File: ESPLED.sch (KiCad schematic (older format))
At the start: 20 parts, among them CON1 BARREL_JACK, P1 PROG, P2 LED_CON, P3 LED_CON_SCREW, P4 LED_CON_SCREW, Q1 IRLZ34N, Q2 IRLZ34N, Q3 IRLZ34N, SW1 Reset, U1 LM1117-3.3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

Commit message: All coponents set
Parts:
- removed P1: PROG, Pin_Headers:Pin_Header_Straight_2x03_Pitch2.54mm, symbol CONN_02X03
- added D?: 1N5819, Diodes_THT:D_DO-41_SOD81_Horizontal_RM10, symbol 1N5819
- added J1: USB_B_Micro, symbol USB_B_Micro
- added R6, R7: R, symbol R
- added SW2: Program, symbol SW_Push
- added U3: INTERFACE-CH340T_SSOP20_, symbol INTERFACE-CH340T_SSOP20_
- added Y1: Crystal, symbol Crystal
- Q1, Q3: symbol Q_NMOS_DGS -> IRLZ34N
- R1, R2, R3: value 4.7k -> 100
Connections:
- net labels added: RXD, TXD, VUSB
- wire segments 60 -> 84
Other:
- moved on the sheet: C1, C2, C3, C4, CON1, P2, P3, P4, Q2, R1, R2, R3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

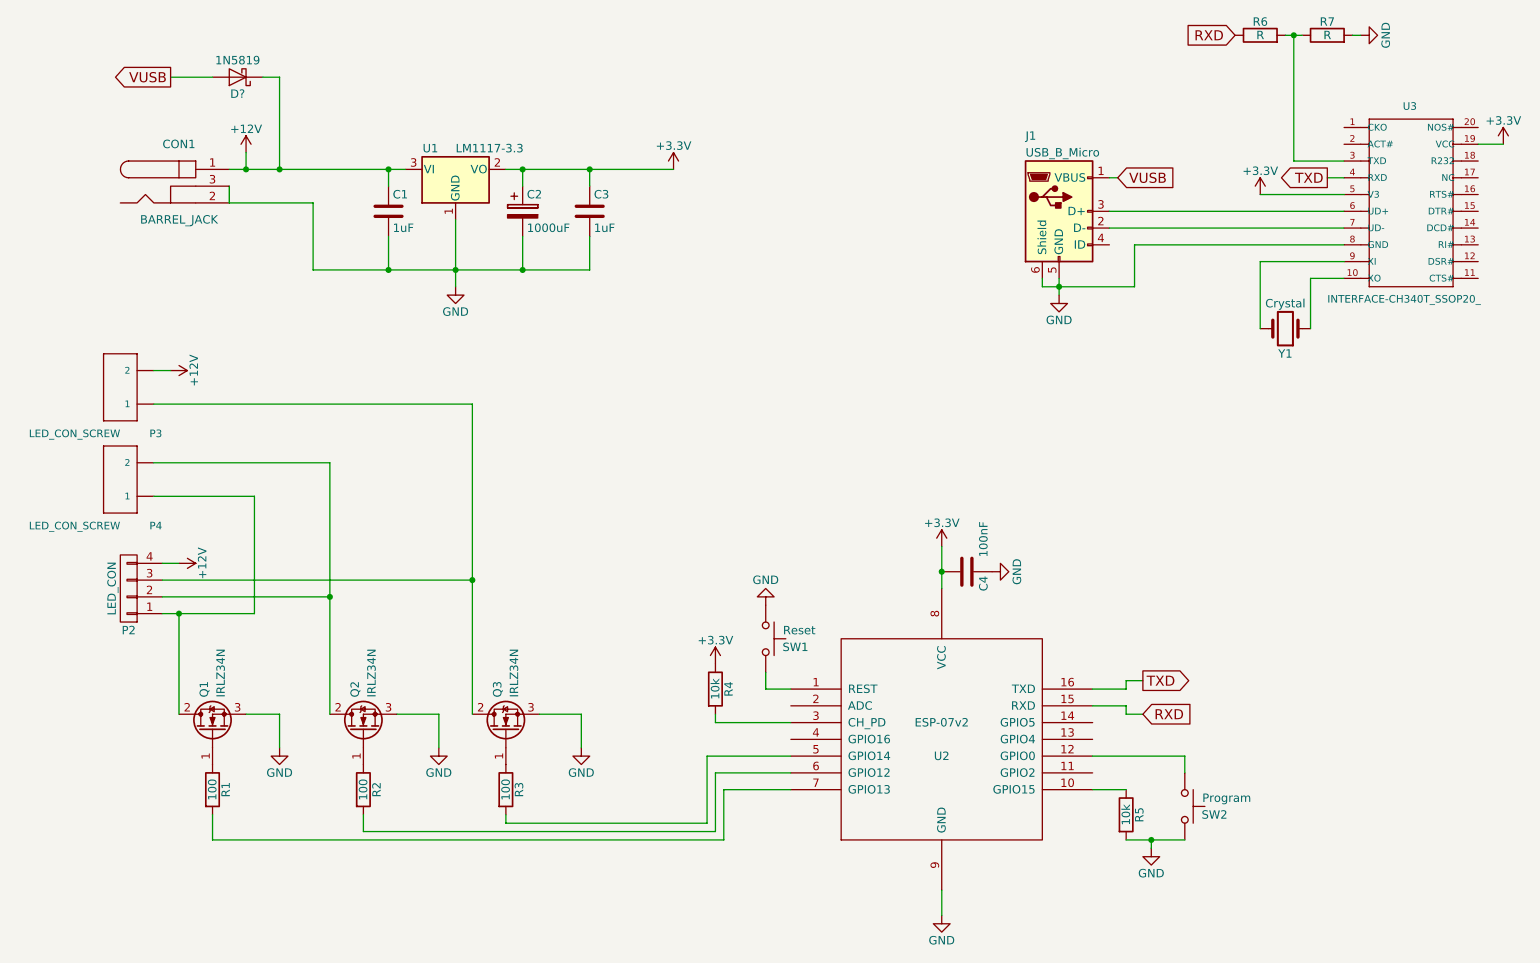
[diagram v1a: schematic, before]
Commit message: Added power suply switching circuit, cleaned up
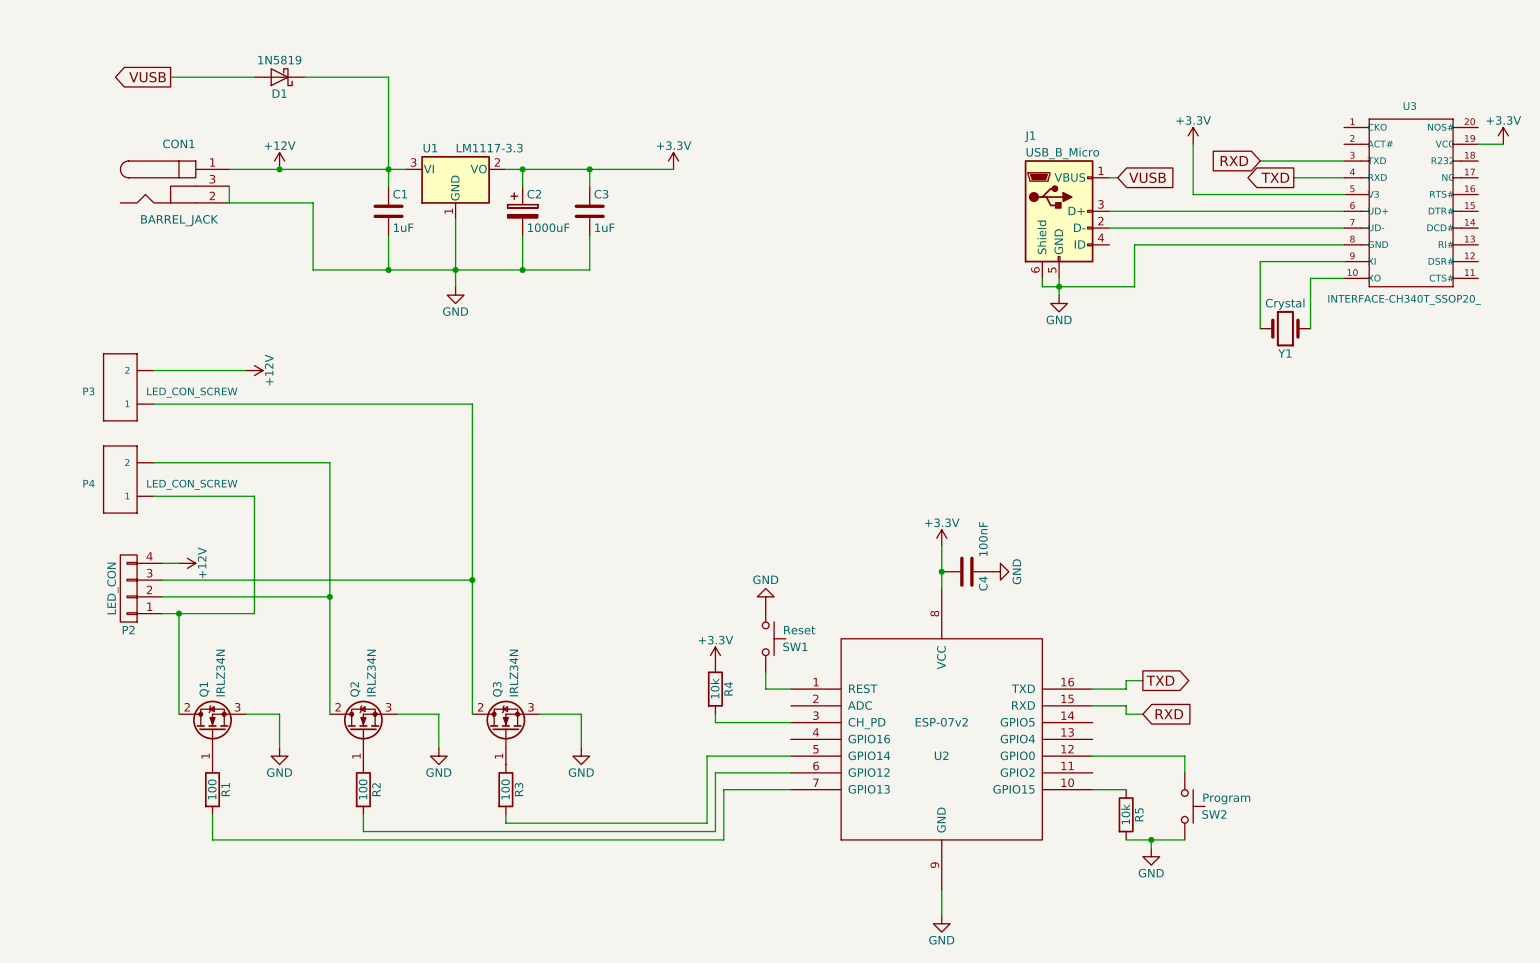
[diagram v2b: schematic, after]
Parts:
- removed R6, R7: R, symbol R
- gave numbers to parts that had none: 1
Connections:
- net RXD: now also U3.3 (TXD)
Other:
- moved on the sheet: D1
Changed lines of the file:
@@
 $EndComp
 Wire Wire Line
-	3050 1800 3050 1900
+	3050 1250 3050 1900
 Wire Wire Line
 	3050 2200 3050 2400
@@
 $EndComp
 Wire Wire Line
-	2100 1800 3150 1800
-Wire Wire Line
 	2100 2000 2600 2000
 Wire Wire Line
@@
 Wire Wire Line
 	6350 6100 6350 6250
-$Comp
-L +12V #PWR03
-U 1 1 5967C962
-P 2200 1700
-F 0 "#PWR03" H 2200 1550 50  0001 C CNN
-F 1 "+12V" H 2200 1840 50  0000 C CNN
-F 2 "" H 2200 1700 50  0000 C CNN
-F 3 "" H 2200 1700 50  0000 C CNN
-	1    2200 1700
-	1    0    0    -1
-$EndComp
 $Comp
 L +3.3V #PWR04
@@
 U 1 1 5A986FD8
 P 1450 3650
-F 0 "P4" H 1200 3900 45  0000 L BNN
-F 1 "LED_CON_SCREW" H 1450 3900 45  0000 L BNN
+F 0 "P4" H 1600 3650 45  0000 L BNN
+F 1 "LED_CON_SCREW" H 750 3650 45  0000 L BNN
 F 2 "SeeedOPL-Connector:H2-3.5-7.0X7.0MM" H 1450 3650 60  0001 C CNN
 F 3 "" H 1450 3650 60  0001 C CNN
@@
 U 1 1 5A987158
 P 1450 3100
-F 0 "P3" H 1200 3350 45  0000 L BNN
-F 1 "LED_CON_SCREW" H 1450 3350 45  0000 L BNN
+F 0 "P3" H 1600 3100 45  0000 L BNN
+F 1 "LED_CON_SCREW" H 750 3100 45  0000 L BNN
 F 2 "SeeedOPL-Connector:H2-3.5-7.0X7.0MM" H 1450 3100 60  0001 C CNN
 F 3 "" H 1450 3100 60  0001 C CNN
@@
 $EndComp
 Wire Wire Line
-	1650 3000 1750 3000
+	1650 3000 2200 3000
 Wire Wire Line
 	1650 3200 3550 3200
@@
 Wire Wire Line
 	7450 5000 7250 5000
-Text GLabel 8650 1850 0    60   Output ~ 0
+Text GLabel 8450 1850 0    60   Output ~ 0
 TXD
-Text GLabel 8100 1000 0    60   Input ~ 0
+Text GLabel 8250 1750 0    60   Input ~ 0
 RXD
-$Comp
-L R R6
-U 1 1 5BF92A24
-P 8250 1000
-F 0 "R6" V 8330 1000 50  0000 C CNN
-F 1 "R" V 8250 1000 50  0000 C CNN
-F 2 "" V 8180 1000 50  0001 C CNN
-F 3 "" H 8250 1000 50  0001 C CNN
-	1    8250 1000
-	0    -1   -1   0
-$EndComp
-$Comp
-L R R7
-U 1 1 5BF92B09
-P 8650 1000
-F 0 "R7" V 8730 1000 50  0000 C CNN
-F 1 "R" V 8650 1000 50  0000 C CNN
-F 2 "" V 8580 1000 50  0001 C CNN
-F 3 "" H 8650 1000 50  0001 C CNN
-	1    8650 1000
-	0    -1   -1   0
-$EndComp
-$Comp
-L GND #PWR015
-U 1 1 5BF92C41
-P 8850 1000
-F 0 "#PWR015" H 8850 750 50  0001 C CNN
-F 1 "GND" H 8850 850 50  0000 C CNN
-F 2 "" H 8850 1000 50  0001 C CNN
-F 3 "" H 8850 1000 50  0001 C CNN
-	1    8850 1000
-	0    -1   -1   0
-$EndComp
-Wire Wire Line
-	8800 1000 8850 1000
-Wire Wire Line
-	8400 1000 8500 1000
-Wire Wire Line
-	8450 1000 8450 1750
-Wire Wire Line
-	8450 1750 8750 1750
-Connection ~ 8450 1000
-Wire Wire Line
-	8650 1850 8750 1850
+Wire Wire Line
+	8450 1850 8750 1850
 Wire Wire Line
 	9700 1650 9550 1650
@@
 	8250 2350 8750 2350
 Wire Wire Line
-	8250 1950 8750 1950
+	7850 1950 8750 1950
 Text GLabel 7400 1850 2    60   Input ~ 0
 VUSB
@@
 L +3.3V #PWR?
 U 1 1 5BF96A99
-P 8250 1950
-F 0 "#PWR?" H 8250 1800 50  0001 C CNN
-F 1 "+3.3V" H 8250 2090 50  0000 C CNN
-F 2 "" H 8250 1950 50  0001 C CNN
-F 3 "" H 8250 1950 50  0001 C CNN
-	1    8250 1950
-	1    0    0    -1
-$EndComp
-$Comp
-L 1N5819 D?
+P 7850 1650
+F 0 "#PWR?" H 7850 1500 50  0001 C CNN
+F 1 "+3.3V" H 7850 1790 50  0000 C CNN
+F 2 "" H 7850 1650 50  0001 C CNN
+F 3 "" H 7850 1650 50  0001 C CNN
+	1    7850 1650
+	1    0    0    -1
+$EndComp
+$Comp
+L 1N5819 D1
 U 1 1 5BF96FE8
-P 2150 1250
-F 0 "D?" H 2150 1350 50  0000 C CNN
-F 1 "1N5819" H 2150 1150 50  0000 C CNN
-F 2 "Diodes_THT:D_DO-41_SOD81_Horizontal_RM10" H 2150 1075 50  0001 C CNN
-F 3 "" H 2150 1250 50  0001 C CNN
-	1    2150 1250
+P 2400 1250
+F 0 "D1" H 2400 1350 50  0000 C CNN
+F 1 "1N5819" H 2400 1150 50  0000 C CNN
+F 2 "Diodes_THT:D_DO-41_SOD81_Horizontal_RM10" H 2400 1075 50  0001 C CNN
+F 3 "" H 2400 1250 50  0001 C CNN
+	1    2400 1250
 	-1   0    0    1
 $EndComp
 Wire Wire Line
-	1750 1250 2000 1250
-Wire Wire Line
-	2300 1250 2400 1250
-Wire Wire Line
-	2400 1250 2400 1800
-Connection ~ 2400 1800
-Wire Wire Line
-	2200 1700 2200 1800
-Connection ~ 2200 1800
+	1750 1250 2250 1250
+Wire Wire Line
+	2550 1250 3050 1250
 $Comp
 L +12V #PWR013
 U 1 1 5A9872D9
-P 1750 3000
-F 0 "#PWR013" H 1750 2850 50  0001 C CNN
-F 1 "+12V" H 1750 3140 50  0000 C CNN
-F 2 "" H 1750 3000 50  0001 C CNN
-F 3 "" H 1750 3000 50  0001 C CNN
-	1    1750 3000
+P 2200 3000
+F 0 "#PWR013" H 2200 2850 50  0001 C CNN
+F 1 "+12V" H 2200 3140 50  0000 C CNN
+F 2 "" H 2200 3000 50  0001 C CNN
+F 3 "" H 2200 3000 50  0001 C CNN
+	1    2200 3000
 	0    1    1    0
 $EndComp
@@
 Wire Wire Line
 	7800 5300 7250 5300
+Wire Wire Line
+	8250 1750 8750 1750
+Wire Wire Line
+	7850 1950 7850 1650
+$Comp
+L +12V #PWR?
+U 1 1 5BFA068F
+P 2400 1800
+F 0 "#PWR?" H 2400 1650 50  0001 C CNN
+F 1 "+12V" H 2400 1940 50  0000 C CNN
+F 2 "" H 2400 1800 50  0001 C CNN
+F 3 "" H 2400 1800 50  0001 C CNN
+	1    2400 1800
+	1    0    0    -1
+$EndComp
+Wire Wire Line
+	2100 1800 3150 1800
+Connection ~ 2400 1800
 $EndSCHEMATC
